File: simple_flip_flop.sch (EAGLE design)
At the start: 33 parts, among them T10 BC847, T11 BC847, T12 BC847, T13 BC847, T14 BC847, T2 BC847, T3 BC847, T4 BC847, T5 BC847, T6 BC847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

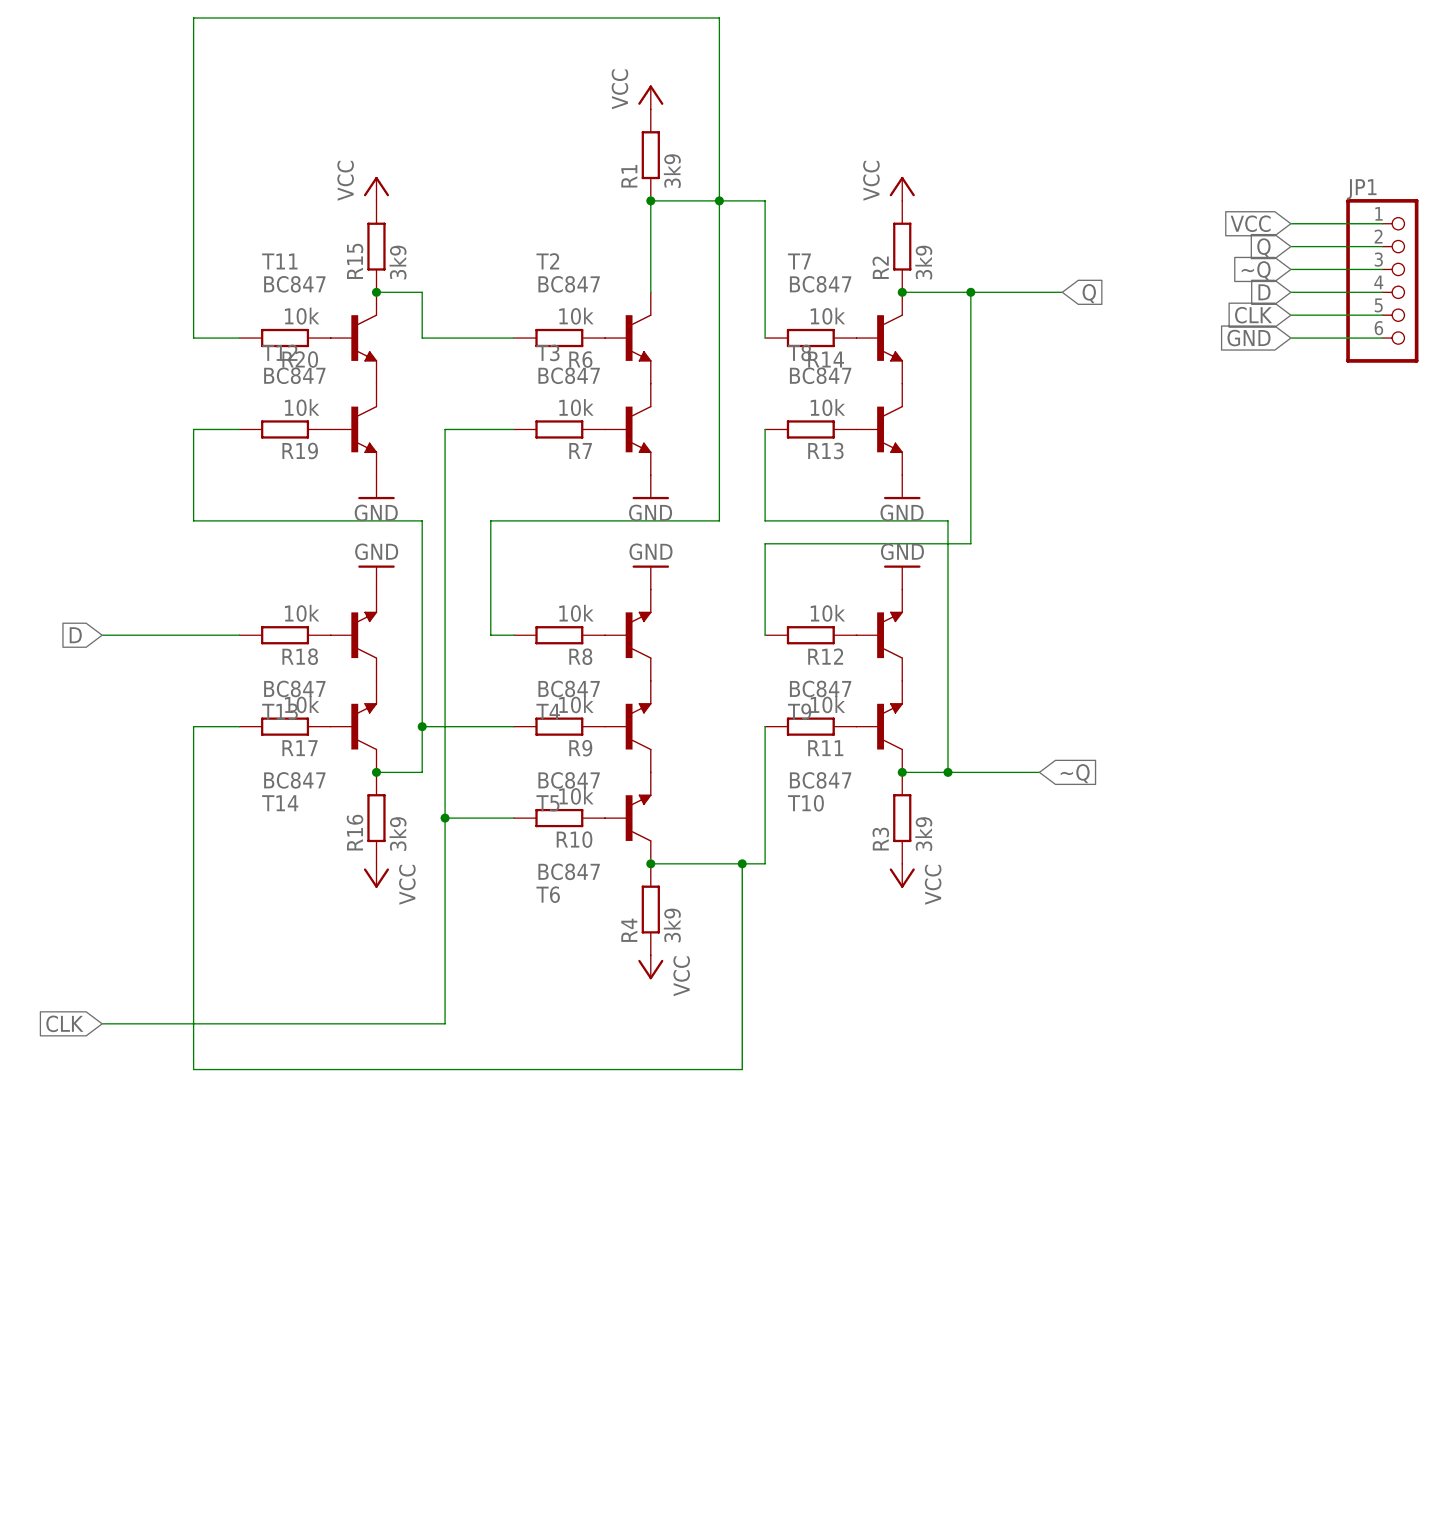
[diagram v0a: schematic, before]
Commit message: prototype board simple_flip_flop
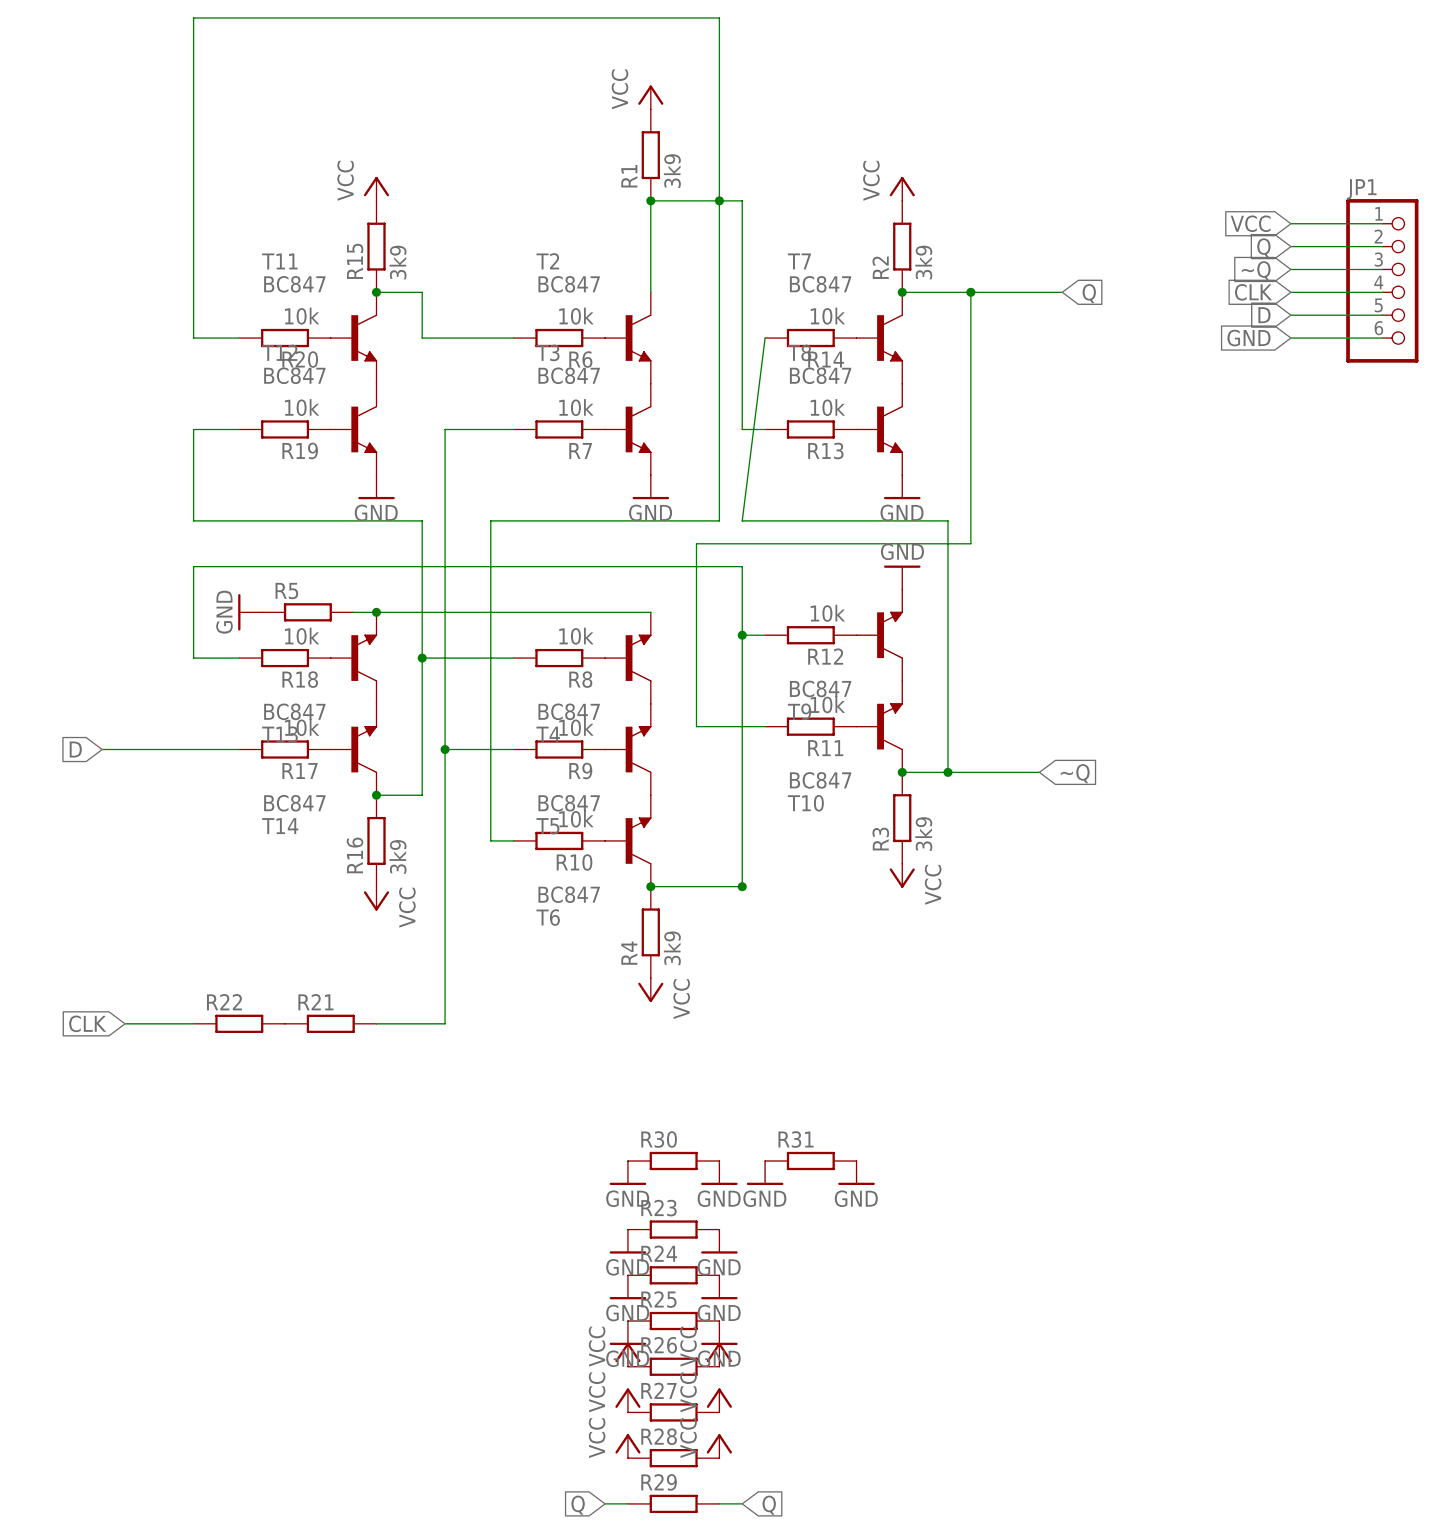
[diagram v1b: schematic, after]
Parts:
- added R21, R22, R23, R24, R25, R26, R27, R28, R30, R31, R5: (no value), resistor:R-EU_R1206
- added R29: (no value), rcl:R-EU_R1206
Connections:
- new net N$1: R5.2, T13.E, T4.E
- new net N$8: R21.1, R22.2
- new net S%9: R21.2, R7.2, R9.2
- net CLK: now also JP1.4, R22.1; no longer JP1.5, R10.2, R7.2
- net D: now also JP1.5, R17.2; no longer JP1.4, R18.2
- net GND: now also R23.1, R23.2, R24.1, R24.2, R25.1, R25.2, R30.1, R30.2, R31.1, R31.2, R5.1; no longer T13.E, T4.E
- net N$10: now also R12.2, R18.2; no longer R11.2, R17.2
- net N$27: now also R8.2; no longer R9.2
- net N$7: now also R10.2, R13.2; no longer R14.2, R8.2
- net Q: now also R11.2, R29.1, R29.2; no longer R12.2
- net VCC: now also R26.1, R26.2, R27.1, R27.2, R28.1, R28.2
- net ~Q: now also R14.2; no longer R13.2
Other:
- moved on the sheet: R10, R16, R17, R18, R4, R8, R9, T13, T14, T4, T5, T6
